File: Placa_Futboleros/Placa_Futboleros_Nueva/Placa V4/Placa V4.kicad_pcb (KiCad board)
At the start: 2 copper layers, 110 x 60 mm, 24 parts, among them J1 LiPo, J2 MI_Ad, J3 MI_At, J4 MD_Ad, J5 MD_At, J6 Pilas, U1 ESP32_30p, U2 DRV8833, U3 DRV8833, U5 ACS712

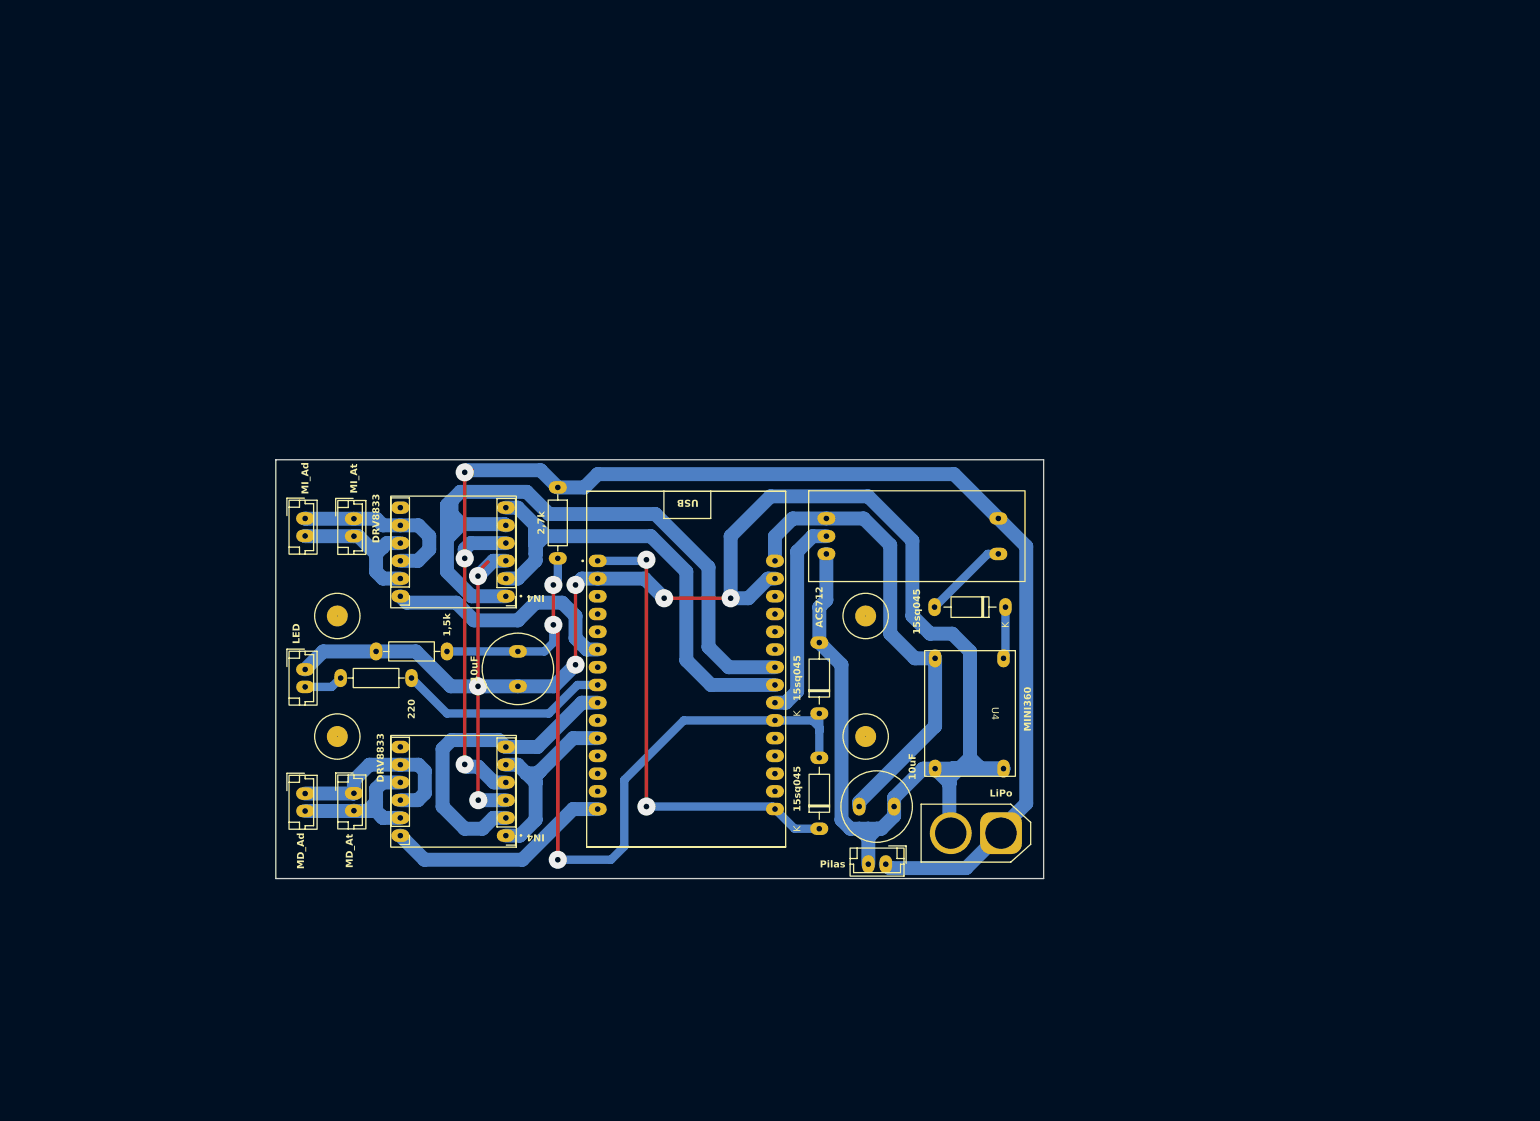
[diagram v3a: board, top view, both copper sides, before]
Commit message: Actualización placa V4
Se reacomoda los componentes y pistas para adaptar el tamaño de la placa
a las placas que poseemos. La placa ahora es de 100mm x 70mm siendo las
compradas de 100mm x 100mm de forma que entra bien.

Las poistas anchas de los motores/drivers y las baterías son de 2,2mm
para una corriente aprox de 7A. El resto son de 1,2mm.

Se adiciona la impresión de las placas en la carpeta de los PDF's, como
también se descarghó en la librería de las placas en la de la ESP, una
imagen con su pinout para evitar confusiones,. y, no necesitar investigar
siempre el mismo dato.
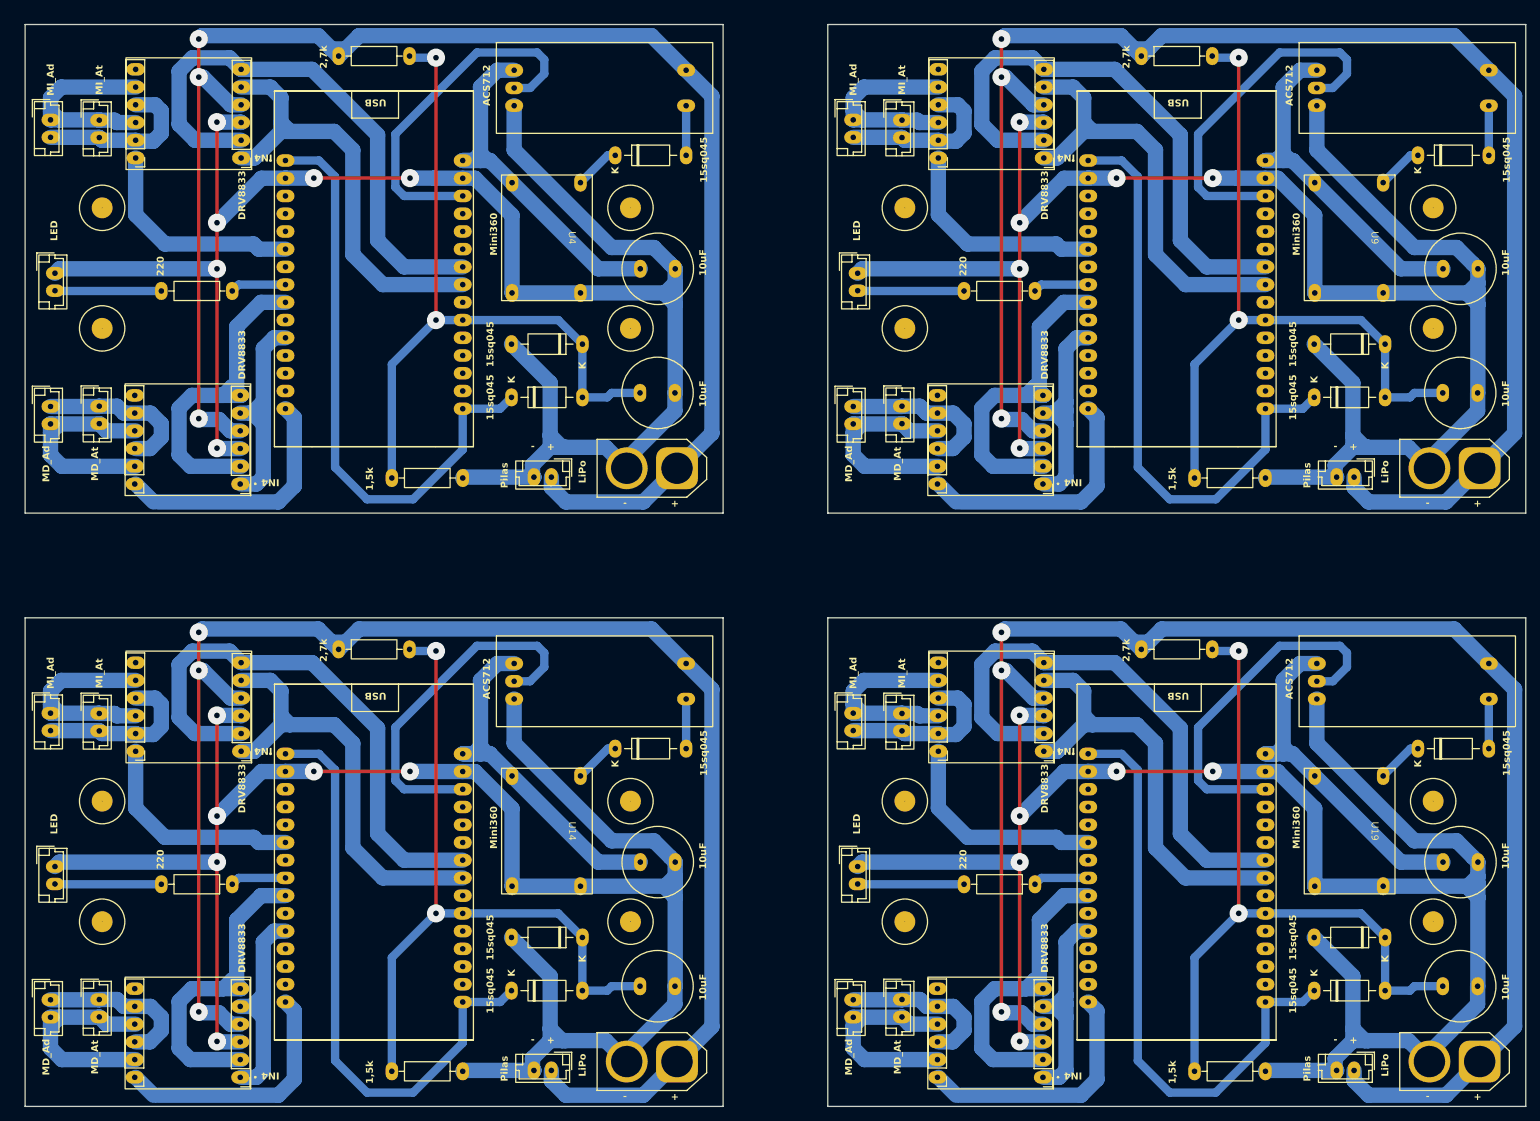
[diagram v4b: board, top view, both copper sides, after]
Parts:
- removed the H2 at (161.5, 127.3)
- removed the H2 at (161.5, 110.0)
- removed the H2 at (85.8, 110.0)
- removed the H2 at (85.8, 127.3)
- added C10: 10uF, Capacitor_THT:C_Radial_D10.0mm_H12.5mm_P5.00mm, F.Cu at (129.2, 163.0)
- added C5: 10uF, Capacitor_THT:C_Radial_D10.0mm_H12.5mm_P5.00mm, F.Cu at (129.2, 60.2)
- added C6: 10uF, Capacitor_THT:C_Radial_D10.0mm_H12.5mm_P5.00mm, F.Cu at (129.2, 78.0)
- added C7: 10uF, Capacitor_THT:C_Radial_D10.0mm_H12.5mm_P5.00mm, F.Cu at (244.2, 60.2)
- added C8: 10uF, Capacitor_THT:C_Radial_D10.0mm_H12.5mm_P5.00mm, F.Cu at (244.2, 78.0)
- added C9: 10uF, Capacitor_THT:C_Radial_D10.0mm_H12.5mm_P5.00mm, F.Cu at (129.2, 145.2)
- added D1: 15sq045, Diode_THT:D_DO-41_SOD81_P10.16mm_Horizontal, F.Cu at (125.6, 44.0)
- added D10: 15sq045, Diode_THT:D_DO-41_SOD81_P10.16mm_Horizontal, F.Cu at (110.8, 163.7)
- added D11: 15sq045, Diode_THT:D_DO-41_SOD81_P10.16mm_Horizontal, F.Cu at (120.9, 156.0)
- added D12: LED, Connector_JST:JST_EH_B2B-EH-A_1x02_P2.50mm_Vertical, F.Cu at (45.3, 145.9)
- added D2: 15sq045, Diode_THT:D_DO-41_SOD81_P10.16mm_Horizontal, F.Cu at (110.8, 78.7)
- added D3: 15sq045, Diode_THT:D_DO-41_SOD81_P10.16mm_Horizontal, F.Cu at (120.9, 71.0)
- added D4: LED, Connector_JST:JST_EH_B2B-EH-A_1x02_P2.50mm_Vertical, F.Cu at (45.3, 60.9)
- added D5: 15sq045, Diode_THT:D_DO-41_SOD81_P10.16mm_Horizontal, F.Cu at (240.6, 44.0)
- added D6: 15sq045, Diode_THT:D_DO-41_SOD81_P10.16mm_Horizontal, F.Cu at (225.8, 78.7)
- added D7: 15sq045, Diode_THT:D_DO-41_SOD81_P10.16mm_Horizontal, F.Cu at (235.9, 71.0)
- added D8: LED, Connector_JST:JST_EH_B2B-EH-A_1x02_P2.50mm_Vertical, F.Cu at (160.3, 60.9)
- added D9: 15sq045, Diode_THT:D_DO-41_SOD81_P10.16mm_Horizontal, F.Cu at (125.6, 129.0)
- added H10: MountingHole, Futboleros:MountingHole_3mm, F.Cu at (127.8, 136.5)
- added H11: MountingHole, Futboleros:MountingHole_3mm, F.Cu at (167.1, 153.8)
- added H12: MountingHole, Futboleros:MountingHole_3mm, F.Cu at (242.8, 153.8)
- added H13: MountingHole, Futboleros:MountingHole_3mm, F.Cu at (167.1, 136.5)
- added H14: MountingHole, Futboleros:MountingHole_3mm, F.Cu at (242.8, 136.5)
- added H2: MountingHole, Futboleros:MountingHole_3mm, F.Cu at (52.1, 68.8)
- added H2: MountingHole, Futboleros:MountingHole_3mm, F.Cu at (127.8, 68.8)
- added H2: MountingHole, Futboleros:MountingHole_3mm, F.Cu at (52.1, 51.5)
- added H2: MountingHole, Futboleros:MountingHole_3mm, F.Cu at (127.8, 51.5)
- added H3: MountingHole, Futboleros:MountingHole_3mm, F.Cu at (167.1, 68.8)
- added H4: MountingHole, Futboleros:MountingHole_3mm, F.Cu at (242.8, 68.8)
- added H5: MountingHole, Futboleros:MountingHole_3mm, F.Cu at (167.1, 51.5)
- added H6: MountingHole, Futboleros:MountingHole_3mm, F.Cu at (242.8, 51.5)
- added H7: MountingHole, Futboleros:MountingHole_3mm, F.Cu at (52.1, 153.8)
- added H8: MountingHole, Futboleros:MountingHole_3mm, F.Cu at (127.8, 153.8)
- added H9: MountingHole, Futboleros:MountingHole_3mm, F.Cu at (52.1, 136.5)
- added J1: LiPo, Connector_AMASS:AMASS_XT60-F_1x02_P7.20mm_Vertical, F.Cu at (134.5, 88.8)
- added J10: MD_Ad, Connector_JST:JST_EH_B2B-EH-A_1x02_P2.50mm_Vertical, F.Cu at (159.7, 80.0)
- added J11: MD_At, Connector_JST:JST_EH_B2B-EH-A_1x02_P2.50mm_Vertical, F.Cu at (166.7, 79.9)
- added J12: Pilas, Connector_JST:JST_EH_B2B-EH-A_1x02_P2.50mm_Vertical, F.Cu at (231.5, 90.1)
- added J13: LiPo, Connector_AMASS:AMASS_XT60-F_1x02_P7.20mm_Vertical, F.Cu at (134.5, 173.8)
- added J14: MI_Ad, Connector_JST:JST_EH_B2B-EH-A_1x02_P2.50mm_Vertical, F.Cu at (44.7, 123.9)
- added J15: MI_At, Connector_JST:JST_EH_B2B-EH-A_1x02_P2.50mm_Vertical, F.Cu at (51.7, 123.9)
- added J16: MD_Ad, Connector_JST:JST_EH_B2B-EH-A_1x02_P2.50mm_Vertical, F.Cu at (44.7, 165.0)
- added J17: MD_At, Connector_JST:JST_EH_B2B-EH-A_1x02_P2.50mm_Vertical, F.Cu at (51.7, 164.9)
- added J18: Pilas, Connector_JST:JST_EH_B2B-EH-A_1x02_P2.50mm_Vertical, F.Cu at (116.5, 175.1)
- added J2: MI_Ad, Connector_JST:JST_EH_B2B-EH-A_1x02_P2.50mm_Vertical, F.Cu at (44.7, 38.9)
- added J3: MI_At, Connector_JST:JST_EH_B2B-EH-A_1x02_P2.50mm_Vertical, F.Cu at (51.7, 38.9)
- added J4: MD_Ad, Connector_JST:JST_EH_B2B-EH-A_1x02_P2.50mm_Vertical, F.Cu at (44.7, 80.0)
- added J5: MD_At, Connector_JST:JST_EH_B2B-EH-A_1x02_P2.50mm_Vertical, F.Cu at (51.7, 79.9)
- added J6: Pilas, Connector_JST:JST_EH_B2B-EH-A_1x02_P2.50mm_Vertical, F.Cu at (116.5, 90.1)
- added J7: LiPo, Connector_AMASS:AMASS_XT60-F_1x02_P7.20mm_Vertical, F.Cu at (249.5, 88.8)
- added J8: MI_Ad, Connector_JST:JST_EH_B2B-EH-A_1x02_P2.50mm_Vertical, F.Cu at (159.7, 38.9)
- added J9: MI_At, Connector_JST:JST_EH_B2B-EH-A_1x02_P2.50mm_Vertical, F.Cu at (166.7, 38.9)
- added R1: 220, Resistor_THT:R_Axial_DIN0207_L6.3mm_D2.5mm_P10.16mm_Horizontal, F.Cu at (70.7, 63.4)
- added R2: 2,7k, Resistor_THT:R_Axial_DIN0207_L6.3mm_D2.5mm_P10.16mm_Horizontal, F.Cu at (86.0, 29.8)
- added R3: 1,5k, Resistor_THT:R_Axial_DIN0207_L6.3mm_D2.5mm_P10.16mm_Horizontal, F.Cu at (93.6, 90.2)
- added R4: 220, Resistor_THT:R_Axial_DIN0207_L6.3mm_D2.5mm_P10.16mm_Horizontal, F.Cu at (185.7, 63.4)
- added R5: 2,7k, Resistor_THT:R_Axial_DIN0207_L6.3mm_D2.5mm_P10.16mm_Horizontal, F.Cu at (201.0, 29.8)
- added R6: 1,5k, Resistor_THT:R_Axial_DIN0207_L6.3mm_D2.5mm_P10.16mm_Horizontal, F.Cu at (208.6, 90.2)
- added R7: 220, Resistor_THT:R_Axial_DIN0207_L6.3mm_D2.5mm_P10.16mm_Horizontal, F.Cu at (70.7, 148.4)
- added R8: 2,7k, Resistor_THT:R_Axial_DIN0207_L6.3mm_D2.5mm_P10.16mm_Horizontal, F.Cu at (86.0, 114.8)
- added R9: 1,5k, Resistor_THT:R_Axial_DIN0207_L6.3mm_D2.5mm_P10.16mm_Horizontal, F.Cu at (93.6, 175.2)
- added U1: ESP32_30p, MODULE_ESP32_DEVKIT_V1:MODULE_ESP32_DEVKIT_V1, F.Cu at (91.1, 60.2)
- added U10: ACS712, SensorCorriente:SensorCorr, F.Cu at (239.1, 34.3)
- added U11: ESP32_30p, MODULE_ESP32_DEVKIT_V1:MODULE_ESP32_DEVKIT_V1, F.Cu at (91.1, 145.2)
- added U12: DRV8833, DRV8833:DRV8833, F.Cu at (64.1, 113.1)
- added U13: DRV8833, DRV8833:DRV8833, F.Cu at (64.0, 159.8)
- added U14: ~, Mini360:Sin título, F.Cu at (115.8, 140.8)
- added U15: ACS712, SensorCorriente:SensorCorr, F.Cu at (124.1, 119.3)
- added U2: DRV8833, DRV8833:DRV8833, F.Cu at (64.1, 28.1)
- added U3: DRV8833, DRV8833:DRV8833, F.Cu at (64.0, 74.8)
- added U4: ~, Mini360:Sin título, F.Cu at (115.8, 55.8)
- added U5: ACS712, SensorCorriente:SensorCorr, F.Cu at (124.1, 34.3)
- added U6: ESP32_30p, MODULE_ESP32_DEVKIT_V1:MODULE_ESP32_DEVKIT_V1, F.Cu at (206.1, 60.2)
- added U7: DRV8833, DRV8833:DRV8833, F.Cu at (179.1, 28.1)
- added U8: DRV8833, DRV8833:DRV8833, F.Cu at (179.0, 74.8)
- added U9: ~, Mini360:Sin título, F.Cu at (230.8, 55.8)
- moved C12 140.9 mm to (244.2, 163.0), turned to 0 degrees
- moved R12 122.8 mm to (208.6, 175.2), turned to 0 degrees
- moved R10 94.1 mm to (185.7, 148.4)
- moved D15 87.2 mm to (235.9, 156.0), turned to 180 degrees
- moved R11 86.8 mm to (201.0, 114.8), turned to 0 degrees
- moved U18 84.4 mm to (179.0, 159.8)
- moved D16 84.0 mm to (160.3, 145.9)
- moved C11 84.0 mm to (244.2, 145.2)
- moved J22 83.9 mm to (159.7, 165.0)
- moved J23 83.9 mm to (166.7, 164.9)
- moved J20 83.3 mm to (159.7, 123.9)
- moved J21 83.3 mm to (166.7, 123.9)
- moved U17 80.2 mm to (179.1, 113.1)
- moved J19 76.0 mm to (249.5, 173.8)
- moved U16 75.5 mm to (206.1, 145.2)
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- renumbered C5 to C11, C6 to C12, D1 to D13, D2 to D14, D3 to D15, D4 to D16, J1 to J19, J2 to J20, J3 to J21, J4 to J22, J5 to J23, J6 to J24, R1 to R10, R2 to R11, R3 to R12, U1 to U16, U2 to U17, U3 to U18, U4 to U19, U5 to U20
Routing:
- net GND: track 313.3 -> 1115.5 mm, vias 7 -> 24
- net VCC: track 204.9 -> 913.0 mm, vias 3 -> 12
- net /ADC: track 122.0 -> 421.1 mm, vias 3 -> 8
- net 3V3: track 68.5 -> 345.5 mm, vias 2 -> 0
- net IN_M1B: track 77.0 -> 320.6 mm
- net Corriente_ADC: track 29.0 -> 206.3 mm
- net IN_M1A: track 102.4 -> 256.7 mm
- net IN_M2B: track 45.1 -> 188.6 mm
- net 5V: track 69.0 -> 211.7 mm
- net SLEEP_M2: track 32.7 -> 142.8 mm
- net IN_M2A: track 30.1 -> 136.4 mm
- net Net-(J4-Pin_2): track 23.4 -> 127.0 mm
- net Net-(J2-Pin_1): track 25.5 -> 120.6 mm
- net SLEEP_M1: track 35.4 -> 126.5 mm
- net Net-(J2-Pin_2): track 23.7 -> 95.2 mm
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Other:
- board size 110 x 60 mm -> 215 x 155 mm
- board text added: "+"
- board text added: "-"
- board text added: "Mini360"
- board text removed: "15sq045"
- board text removed: "MINI360"

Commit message: Actualización 3D placa V4
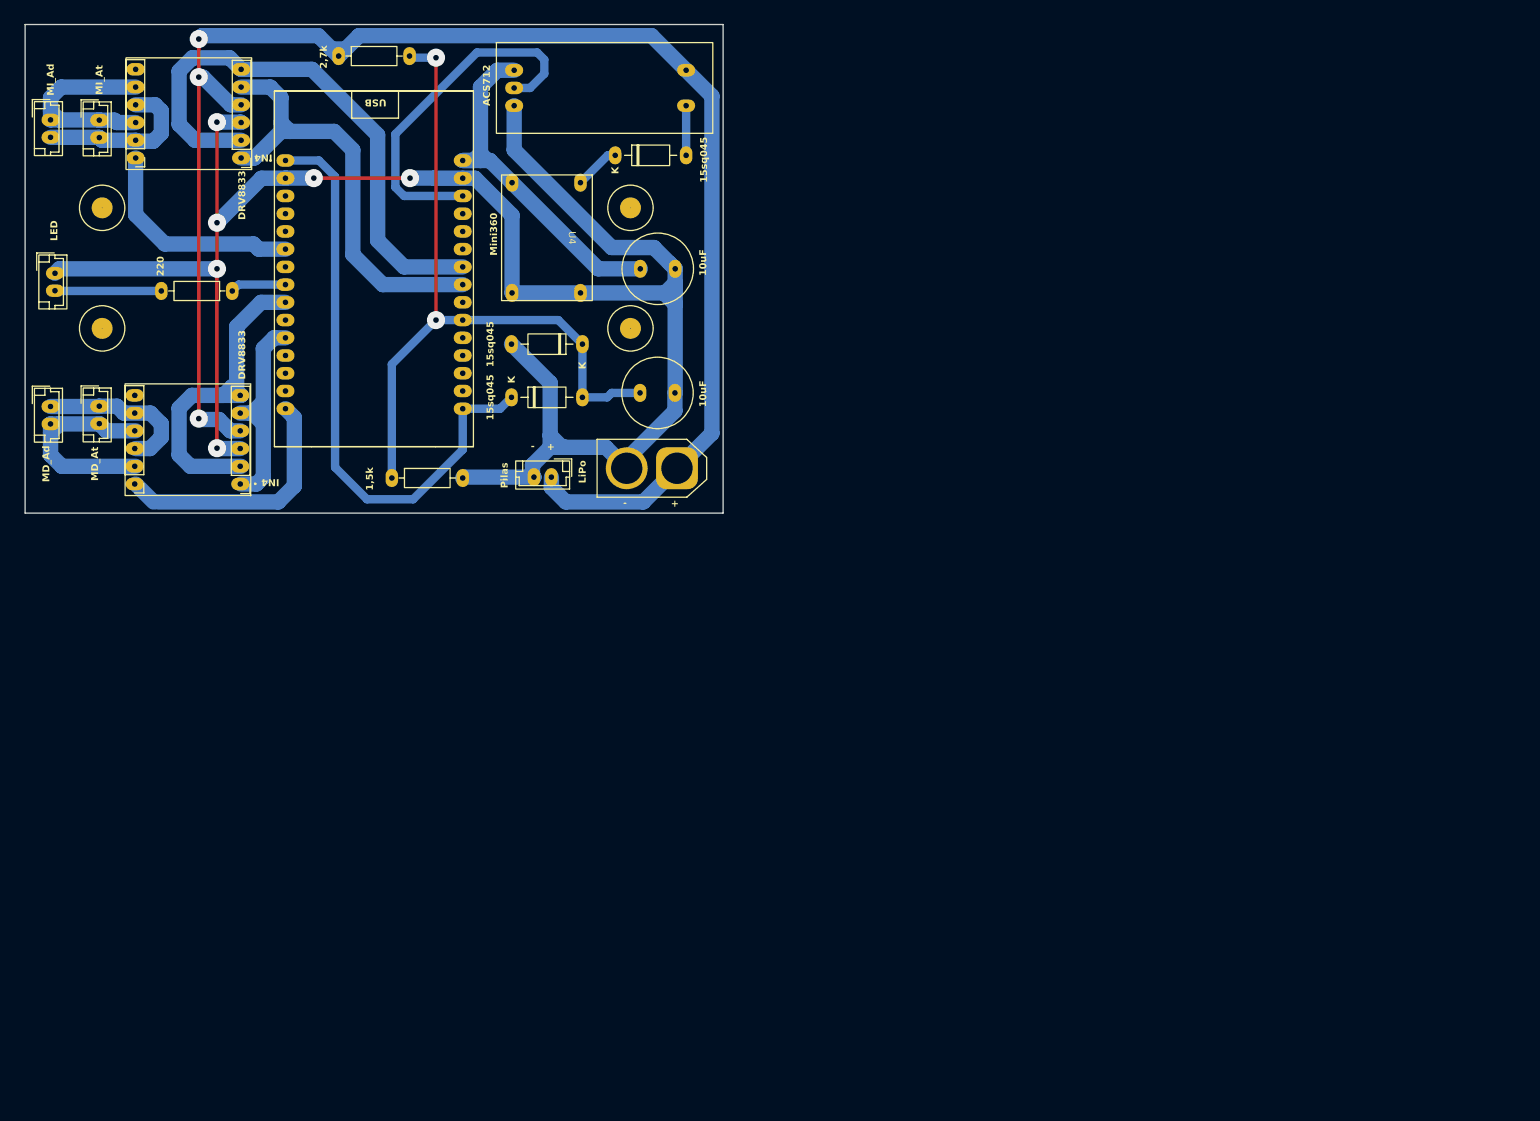
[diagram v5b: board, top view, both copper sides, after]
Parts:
- removed C10, C11, C12, C7, C8, C9: 10uF, Capacitor_THT:C_Radial_D10.0mm_H12.5mm_P5.00mm
- removed D10, D11, D13, D14, D15, D5, D6, D7, D9: 15sq045, Diode_THT:D_DO-41_SOD81_P10.16mm_Horizontal
- removed D12, D16, D8: LED, Connector_JST:JST_EH_B2B-EH-A_1x02_P2.50mm_Vertical
- removed H10, H11, H12, H13, H14, H3, H4, H5, H6, H7, H8, H9: MountingHole, Futboleros:MountingHole_3mm
- removed J10, J16, J22: MD_Ad, Connector_JST:JST_EH_B2B-EH-A_1x02_P2.50mm_Vertical
- removed J11, J17, J23: MD_At, Connector_JST:JST_EH_B2B-EH-A_1x02_P2.50mm_Vertical
- removed J12, J18, J24: Pilas, Connector_JST:JST_EH_B2B-EH-A_1x02_P2.50mm_Vertical
- removed J13, J19, J7: LiPo, Connector_AMASS:AMASS_XT60-F_1x02_P7.20mm_Vertical
- removed J14, J20, J8: MI_Ad, Connector_JST:JST_EH_B2B-EH-A_1x02_P2.50mm_Vertical
- removed J15, J21, J9: MI_At, Connector_JST:JST_EH_B2B-EH-A_1x02_P2.50mm_Vertical
- removed R10, R4, R7: 220, Resistor_THT:R_Axial_DIN0207_L6.3mm_D2.5mm_P10.16mm_Horizontal
- removed R11, R5, R8: 2,7k, Resistor_THT:R_Axial_DIN0207_L6.3mm_D2.5mm_P10.16mm_Horizontal
- removed R12, R6, R9: 1,5k, Resistor_THT:R_Axial_DIN0207_L6.3mm_D2.5mm_P10.16mm_Horizontal
- removed U10, U15, U20: ACS712, SensorCorriente:SensorCorr
- removed U11, U16, U6: ESP32_30p, MODULE_ESP32_DEVKIT_V1:MODULE_ESP32_DEVKIT_V1
- removed U12, U13, U17, U18, U7, U8: DRV8833, DRV8833:DRV8833
- removed U14, U19, U9: ~, Mini360:Sin título
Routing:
- net GND: track 1115.5 -> 278.9 mm, vias 24 -> 6
- net VCC: track 913.0 -> 228.2 mm, vias 12 -> 3
- net /ADC: track 421.1 -> 105.3 mm, vias 8 -> 2
- net 3V3: track 345.5 -> 86.4 mm
- net IN_M1B: track 320.6 -> 80.1 mm
- net IN_M1A: track 256.7 -> 64.2 mm
- net 5V: track 211.7 -> 52.9 mm
- net Corriente_ADC: track 206.3 -> 51.6 mm
- net IN_M2B: track 188.6 -> 47.1 mm
- net SLEEP_M2: track 142.8 -> 35.7 mm
- net IN_M2A: track 136.4 -> 34.1 mm
- net Net-(J4-Pin_2): track 127.0 -> 31.7 mm
- net SLEEP_M1: track 126.5 -> 31.6 mm
- net Net-(J2-Pin_1): track 120.6 -> 30.1 mm
- net Net-(J2-Pin_2): track 95.2 -> 23.8 mm
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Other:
- board size 215 x 155 mm -> 100 x 70 mm

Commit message: Corrección pistas placa V4
Se achican las pistas que estaban engrosadas popr error.
Y se vuelve a exportar el pdf para imprimir.
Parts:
- removed the H2 at (52.1, 68.8)
- removed the H2 at (127.8, 68.8)
- removed the H2 at (52.1, 51.5)
- removed the H2 at (127.8, 51.5)
- added H1: MountingHole, Futboleros:MountingHole_3mm, F.Cu at (126.2, 53.3)
- added H2: MountingHole, Futboleros:MountingHole_3mm, F.Cu at (126.2, 70.6)
- added H3: MountingHole, Futboleros:MountingHole_3mm, F.Cu at (50.5, 70.6)
- added H4: MountingHole, Futboleros:MountingHole_3mm, F.Cu at (50.5, 53.3)
- moved C5 2.39 mm to (127.6, 62.1)
- moved J1 2.39 mm to (132.9, 90.6)
- moved U3 2.39 mm to (62.5, 76.6)
- moved J2 2.39 mm to (43.1, 40.7)
- moved J3 2.39 mm to (50.1, 40.8)
- moved U1 2.39 mm to (89.5, 62.1)
- moved U4 2.39 mm to (114.3, 57.6)
- moved R2 2.39 mm to (84.4, 31.6)
- moved U2 2.39 mm to (62.6, 29.9)
- moved D2 2.39 mm to (109.2, 80.5)
- moved D3 2.39 mm to (119.3, 72.8)
- moved D4 2.39 mm to (43.8, 62.7)
- moved J4 2.39 mm to (43.1, 81.8)
- moved J5 2.39 mm to (50.1, 81.7)
- moved J6 2.39 mm to (114.9, 91.9)
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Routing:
- net IN_M2B: track 47.1 -> 49.6 mm
- net SLEEP_M1: track 31.6 -> 31.0 mm
